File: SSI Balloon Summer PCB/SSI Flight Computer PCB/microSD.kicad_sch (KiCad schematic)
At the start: 5 parts, among them J6 1040310811

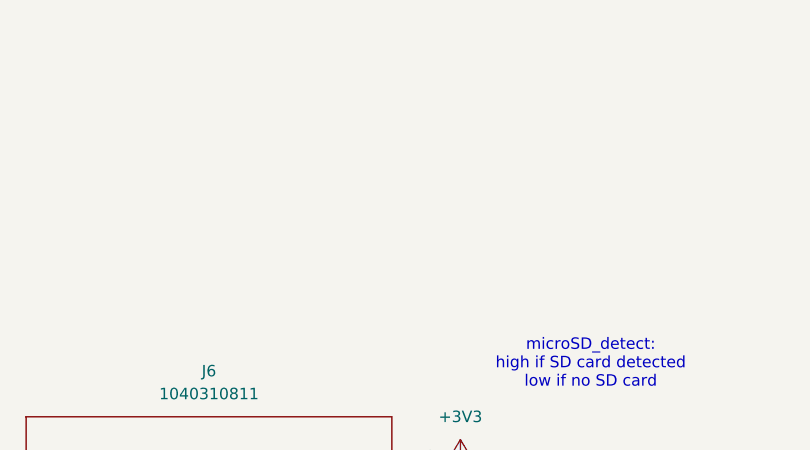
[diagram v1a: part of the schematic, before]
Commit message: Added Headers for testing, finalizing PCB
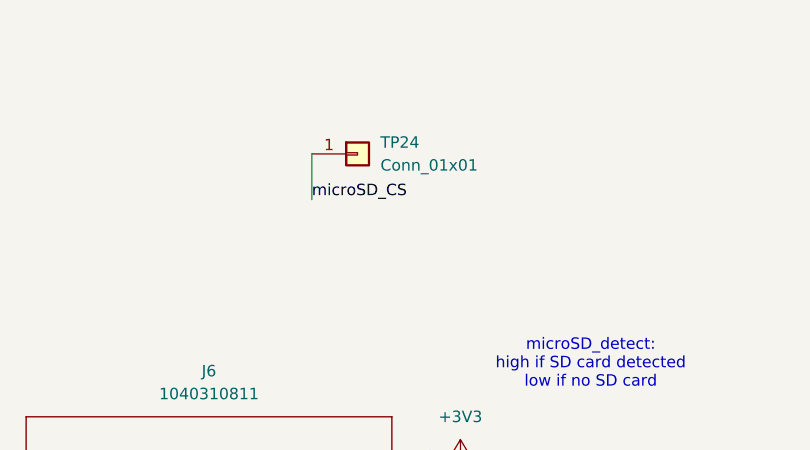
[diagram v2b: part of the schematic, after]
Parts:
- added TP24: Conn_01x01, Connector_PinHeader_2.54mm:PinHeader_1x01_P2.54mm_Vertical, symbol Connector_Generic:Conn_01x01
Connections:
- net microSD_CS: now also TP24.1 (Pin_1)
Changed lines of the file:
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@@
+	(wire
+		(pts
+			(xy 109.22 41.91) (xy 109.22 46.99)
+		)
+		(stroke
+			(width 0)
+			(type default)
+		)
+	)
 	(wire
 		(pts
@@
 			)
 			(justify right bottom)
+		)
+	)
+	(label "microSD_CS"
+		(at 109.22 46.99 0)
+		(effects
+			(font
+				(size 1.27 1.27)
+			)
+			(justify left bottom)
 		)
 	)
@@
 					(unit 1)
 				)
+			)
+		)
+	)
+	(symbol
+		(lib_id "Connector_Generic:Conn_01x01")
+		(at 114.3 41.91 0)
+		(unit 1)
+		(body_style 1)
+		(exclude_from_sim no)
+		(in_bom yes)
+		(on_board yes)
+		(in_pos_files yes)
+		(dnp no)
+		(fields_autoplaced yes)
+		(property "Reference" "TP24"
+			(at 116.84 40.6399 0)
+			(show_name no)
+			(do_not_autoplace no)
+			(effects
+				(font
+					(size 1.27 1.27)
+				)
+				(justify left)
+			)
+		)
+		(property "Value" "Conn_01x01"
+			(at 116.84 43.1799 0)
+			(show_name no)
+			(do_not_autoplace no)
+			(effects
+				(font
+					(size 1.27 1.27)
+				)
+				(justify left)
+			)
+		)
+		(property "Footprint" "Connector_PinHeader_2.54mm:PinHeader_1x01_P2.54mm_Vertical"
+			(at 114.3 41.91 0)
+			(hide yes)
+			(show_name no)
+			(do_not_autoplace no)
+			(effects
+				(font
+					(size 1.27 1.27)
+				)
+			)
+		)
+		(property "Datasheet" ""
+			(at 114.3 41.91 0)
+			(hide yes)
+			(show_name no)
+			(do_not_autoplace no)
+			(effects
+				(font
+					(size 1.27 1.27)
+				)
+			)
+		)
+		(property "Description" "Generic connector, single row, 01x01, script generated (kicad-library-utils/schlib/autogen/connector/)"
+			(at 114.3 41.91 0)
+			(hide yes)
+			(show_name no)
+			(do_not_autoplace no)
+			(effects
+				(font
+					(size 1.27 1.27)
+				)
+			)
+		)
+		(pin "1"
+		)
+		(instances
+			(project "SSI Summer Balloons"
+				(path "/3c45a535-6e6b-4825-ad52-82c10cbe7866/0df234a1-8d04-4ff9-99d5-3634fc842029"
+					(reference "TP24")
+					(unit 1)
+				)

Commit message: More silkscreen organization, combined some pinheaders
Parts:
- TP24: value Conn_01x01 -> microSD_CS
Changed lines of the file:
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@@
 			)
 		)
-		(property "Value" "Conn_01x01"
+		(property "Value" "microSD_CS"
 			(at 116.84 43.1799 0)
 			(show_name no)

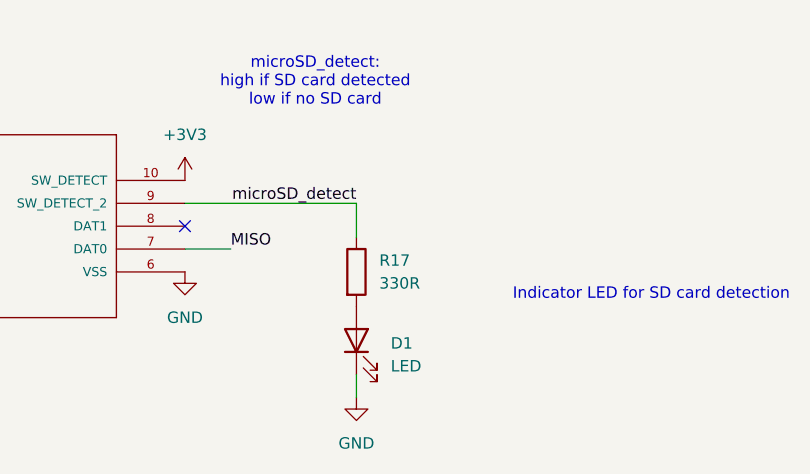
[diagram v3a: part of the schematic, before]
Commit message: finished finding all parts on JLCPCB - finalizing BOM then order
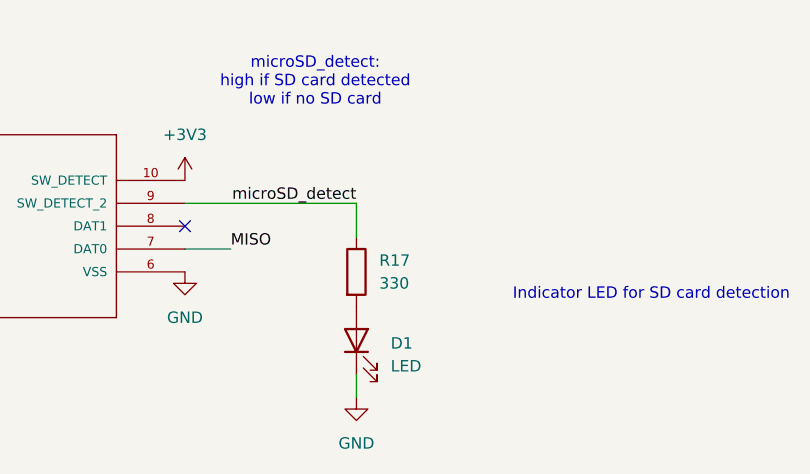
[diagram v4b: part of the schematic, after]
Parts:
- C34: LCSC (none) -> C519438
- D1: LCSC (none) -> C2292
- J6: LCSC (none) -> C585350
- R17: value 330R -> 330; LCSC (none) -> C23138
- R26: LCSC (none) -> C25804
- TP24: LCSC (none) -> C81276
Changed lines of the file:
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@@
+			)
+		)
+		(property "LCSC" "C2292"
+			(at 144.78 93.98 90)
+			(hide yes)
+			(show_name no)
+			(do_not_autoplace no)
+			(effects
+				(font
+					(size 1.27 1.27)
+				)
 			)
 		)
@@
 		)
 		(property "PART_REV" ""
+			(at 62.23 72.39 0)
+			(hide yes)
+			(show_name no)
+			(do_not_autoplace no)
+			(effects
+				(font
+					(size 1.27 1.27)
+				)
+			)
+		)
+		(property "LCSC" "C25804"
 			(at 62.23 72.39 0)
 			(hide yes)
@@
 			)
 		)
-		(property "Datasheet" ""
+		(property "Datasheet" "C81276"
 			(at 114.3 41.91 0)
 			(hide yes)
@@
 		)
 		(property "Description" "Generic connector, single row, 01x01, script generated (kicad-library-utils/schlib/autogen/connector/)"
+			(at 114.3 41.91 0)
+			(hide yes)
+			(show_name no)
+			(do_not_autoplace no)
+			(effects
+				(font
+					(size 1.27 1.27)
+				)
+			)
+		)
+		(property "LCSC" "C81276"
 			(at 114.3 41.91 0)
 			(hide yes)
@@
 			)
 		)
+		(property "LCSC" "C585350"
+			(at 69.85 76.2 0)
+			(hide yes)
+			(show_name no)
+			(do_not_autoplace no)
+			(effects
+				(font
+					(size 1.27 1.27)
+				)
+			)
+		)
 		(pin "7"
 		)
@@
 			)
 		)
+		(property "LCSC" "C519438"
+			(at 41.91 87.63 0)
+			(hide yes)
+			(show_name no)
+			(do_not_autoplace no)
+			(effects
+				(font
+					(size 1.27 1.27)
+				)
+			)
+		)
 		(pin "2"
 		)
@@
 			)
 		)
-		(property "Value" "330R"
+		(property "Value" "330"
 			(at 147.32 87.6299 0)
 			(show_name no)
@@
 			(at 144.78 86.36 0)
 			(hide yes)
+			(show_name no)
+			(do_not_autoplace no)
+			(effects
+				(font
+					(size 1.27 1.27)
+				)
+			)
+		)
+		(property "LCSC" "C23138"
+			(at 144.78 86.36 0)
+			(hide yes)

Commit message: PCB finally done i think and ready to order
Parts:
- removed D1: LED, LED_SMD:LED_0805_2012Metric, symbol Device:LED
- removed R17: 330, Resistor_SMD:R_0603_1608Metric, symbol Device:R
- added C35: 1uF, Capacitor_SMD:C_0603_1608Metric, symbol Device:C
- C34: LCSC C519438 -> C14663
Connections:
- net +3V3: now also C35.1
- net GND: now also C35.2
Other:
- note added: "Indicator LED for SD card detection in STM as GPIO"
- note removed: "Indicator LED for SD card detection"

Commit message: Board done but we have a price crisis so might have to change things
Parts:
- TP24: now not fitted; now left out of the parts list
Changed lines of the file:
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@@
 		(body_style 1)
 		(exclude_from_sim no)
-		(in_bom yes)
+		(in_bom no)
 		(on_board yes)
 		(in_pos_files yes)
-		(dnp no)
+		(dnp yes)
 		(fields_autoplaced yes)
 		(property "Reference" "TP24"
